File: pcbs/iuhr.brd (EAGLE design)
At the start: 38.4 x 23 mm, 82 parts, among them Q1 20.000MHz, Q2 MOSFET-NCHANNELSMD

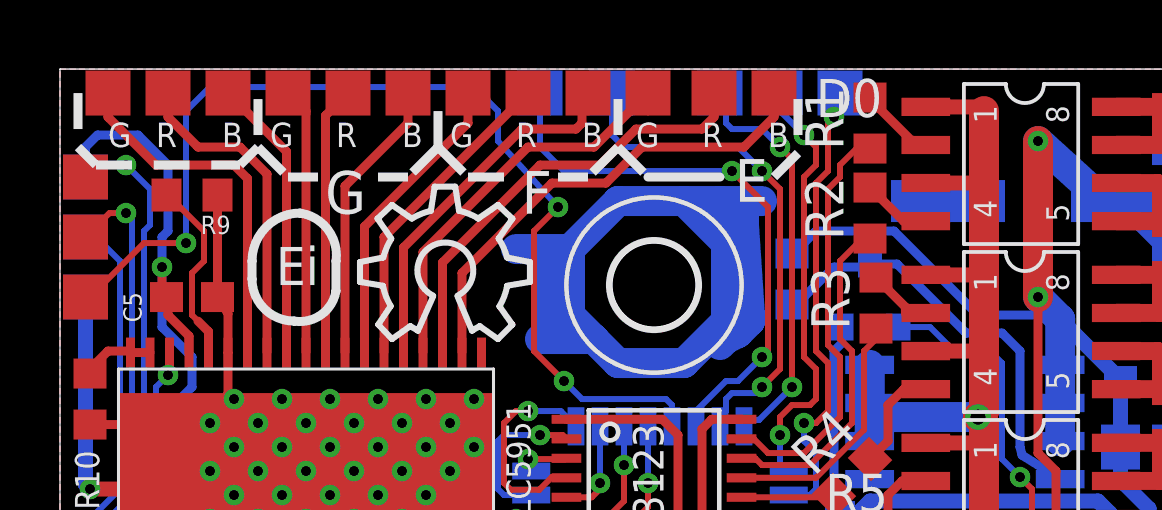
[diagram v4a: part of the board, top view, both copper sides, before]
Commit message: Add GND and +5V breakout pads.
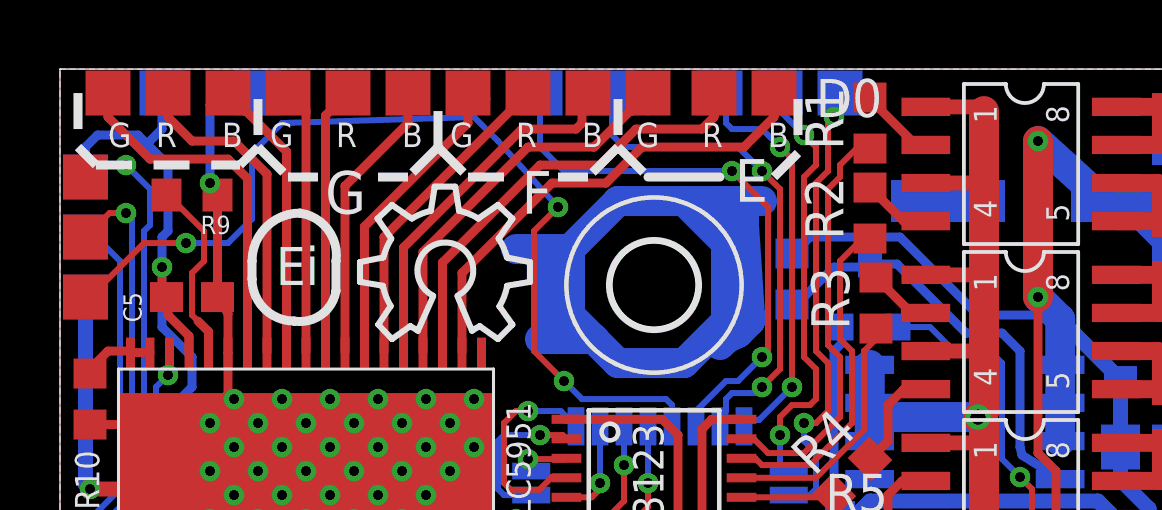
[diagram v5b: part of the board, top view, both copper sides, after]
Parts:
- added +5V, GND: TPTP15SQ, testpad:TP15SQ
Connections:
- net GND: now also GND.TP
- net VCC: now also +5V.TP
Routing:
- net GND: track 149.0 -> 155.2 mm, vias 41 -> 42
- net RESET: track 35.5 -> 32.7 mm
- net VCC: track 65.3 -> 67.2 mm
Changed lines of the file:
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@@
 <text x="38.2" y="21.4" size="0.8128" layer="26" rot="MR0">+12V</text>
 <text x="38" y="12.8" size="0.8128" layer="26" rot="MR0">GND</text>
-<text x="24.2" y="15.6" size="0.8128" layer="26" rot="MR90">Encoder</text>
+<text x="26.4" y="19" size="0.8128" layer="26" rot="MR0">Encoder</text>
 <wire x1="21" y1="22.2" x2="21" y2="20.2" width="0.3" layer="26" style="shortdash"/>
 <wire x1="21" y1="20.2" x2="21.8" y2="19.4" width="0.3" layer="26" style="shortdash"/>
@@
 <wire x1="10.6" y1="22.6" x2="10.6" y2="22" width="0.3" layer="26"/>
 <wire x1="10.6" y1="22" x2="11.2" y2="21.4" width="0.3" layer="26"/>
-<text x="14.8" y="0.4" size="0.8128" layer="26" rot="MR35">https://github.com/ekiwi/iuhr</text>
+<text x="12.8" y="0.6" size="0.6096" layer="26" rot="MR35">https://github.com/ekiwi/iuhr</text>
 <text x="5.2" y="16.8" size="0.8128" layer="26" rot="MR180">(C) eKiwi 2013</text>
 <text x="6" y="15.2" size="0.8128" layer="26" rot="MR180">licensed under
@@
 <text x="21.4" y="20.4" size="0.8128" layer="25">R</text>
 <text x="23.6" y="20.4" size="0.8128" layer="25">B</text>
-<text x="11.8" y="18.4" size="0.8128" layer="26" rot="MR0">powered by
+<text x="13.4" y="17.6" size="0.8128" layer="26" rot="MR0">powered by
 xpcc</text>
+<wire x1="3.6" y1="21.4" x2="4.4" y2="20.6" width="0.3" layer="22"/>
+<wire x1="4.4" y1="20.6" x2="4.4" y2="19.8" width="0.3" layer="22"/>
+<wire x1="4.4" y1="19.8" x2="4" y2="20.2" width="0.3" layer="22"/>
+<wire x1="4.4" y1="19.8" x2="4.8" y2="20.2" width="0.3" layer="22"/>
+<wire x1="6.6" y1="21.4" x2="6.6" y2="20" width="0.3" layer="22"/>
+<wire x1="7" y1="20" x2="6.2" y2="20" width="0.3" layer="22"/>
 </plain>
 <attributes>
@@
 <element name="R7" library="resistor" package="R0603" value="33" x="27.2" y="3.6" rot="R270"/>
 <element name="R8" library="resistor" package="R0603" value="33" x="24" y="4.4" rot="R270"/>
+<element name="+5V" library="testpad" package="TP15SQ" value="TPTP15SQ" x="3.4" y="22.2" smashed="yes" rot="MR0">
+<attribute name="TP_SIGNAL_NAME" value="" x="3.4" y="19.66" size="1" layer="38" rot="MR0"/>
+<attribute name="NAME" x="2.1501" y="21.6001" size="0.8128" layer="26" rot="MR0"/>
+<attribute name="VALUE" x="4.162" y="21.311" size="0.0254" layer="28" rot="MR0"/>
+</element>
+<element name="GND" library="testpad" package="TP15SQ" value="TPTP15SQ" x="6.6" y="22.2" smashed="yes" rot="MR0">
+<attribute name="TP_SIGNAL_NAME" value="" x="6.6" y="19.66" size="1" layer="38" rot="MR0"/>
+<attribute name="NAME" x="10.1501" y="21.8001" size="0.8128" layer="26" rot="MR0"/>
+<attribute name="VALUE" x="7.362" y="21.311" size="0.0254" layer="28" rot="MR0"/>
+</element>
 </elements>
 <signals>
@@
 <wire x1="30.85" y1="4.6" x2="30.85" y2="4.05" width="0.3" layer="16"/>
 <wire x1="30.85" y1="4.05" x2="30.4" y2="3.6" width="0.3" layer="16"/>
+<contactref element="GND" pad="TP"/>
+<wire x1="5.25" y1="18.8" x2="5.25" y2="19.15" width="0.3" layer="1"/>
+<wire x1="5.25" y1="19.15" x2="5" y2="19.2" width="0.3" layer="1"/>
+<via x="5" y="19.2" extent="1-16" drill="0.3302"/>
+<wire x1="5.2" y1="22" x2="6.6" y2="22.2" width="0.3" layer="16"/>
+<wire x1="5" y1="19.2" x2="5" y2="21.8" width="0.3" layer="16"/>
+<wire x1="5" y1="21.8" x2="6.6" y2="22.2" width="0.3" layer="16"/>
 </signal>
 <signal name="VCC">
@@
 <wire x1="3.4" y1="17.4" x2="3.6" y2="17.6" width="0.3" layer="16"/>
 <wire x1="3.6" y1="17.6" x2="3.6" y2="19.8" width="0.3" layer="16"/>
-<wire x1="3.6" y1="19.8" x2="2.6" y2="20.8" width="0.3" layer="16"/>
+<wire x1="3.6" y1="19.8" x2="2.9" y2="20.5" width="0.3" layer="16"/>
+<wire x1="2.9" y1="20.5" x2="2.6" y2="20.8" width="0.3" layer="16"/>
 <wire x1="2.6" y1="20.8" x2="1.25" y2="20.8" width="0.3" layer="16"/>
 <wire x1="1.25" y1="20.8" x2="0.85" y2="20.4" width="0.3" layer="16"/>
@@
 <wire x1="25" y1="5.8" x2="25.45" y2="5.8" width="0.3" layer="16"/>
 <wire x1="25.45" y1="5.8" x2="26" y2="6.35" width="0.3" layer="16"/>
+<contactref element="+5V" pad="TP"/>
+<wire x1="3.4" y1="22.2" x2="3.4" y2="21" width="0.3" layer="16"/>
+<wire x1="3.4" y1="21" x2="2.9" y2="20.5" width="0.3" layer="16"/>
 </signal>
 <signal name="RESET">
@@
 <wire x1="2.8" y1="17.2" x2="4.2" y2="17.2" width="0.2" layer="1"/>
 <wire x1="0.85" y1="15.65" x2="0.85" y2="15.4" width="0.2" layer="1"/>
-<wire x1="4.2" y1="17.2" x2="4.2" y2="21.6" width="0.2" layer="16"/>
-<wire x1="4.2" y1="21.6" x2="5" y2="22.4" width="0.2" layer="16"/>
-<wire x1="5" y1="22.4" x2="13.8" y2="22.4" width="0.2" layer="16"/>
-<wire x1="13.8" y1="22.4" x2="14.6" y2="21.6" width="0.2" layer="16"/>
-<wire x1="14.6" y1="21.6" x2="14.6" y2="20.6" width="0.2" layer="16"/>
+<wire x1="7.4" y1="21.2" x2="13.8" y2="21.4" width="0.2" layer="16"/>
+<wire x1="13.8" y1="21.4" x2="14.6" y2="20.6" width="0.2" layer="16"/>
 <wire x1="17.4" y1="12" x2="16.8" y2="12.6" width="0.2" layer="16"/>
 <via x="16.8" y="12.6" extent="1-16" drill="0.3302"/>
@@
 <via x="16.6" y="18.4" extent="1-16" drill="0.3302"/>
 <wire x1="16.6" y1="18.4" x2="14.6" y2="20.6" width="0.2" layer="16"/>
+<wire x1="4.2" y1="17.2" x2="5.6" y2="17.2" width="0.2" layer="16"/>
+<wire x1="5.6" y1="17.2" x2="6.4" y2="18" width="0.2" layer="16"/>
+<wire x1="6.4" y1="18" x2="6.4" y2="20.2" width="0.2" layer="16"/>
+<wire x1="6.4" y1="20.2" x2="7.4" y2="21.2" width="0.2" layer="16"/>
 </signal>
 <signal name="N$2">
@@
 <contactref element="XR" pad="TP"/>
 <contactref element="TLC5951" pad="31"/>
-<wire x1="4.6" y1="20.4" x2="3.6" y2="21.4" width="0.3" layer="1"/>
+<wire x1="4.4" y1="20.6" x2="3.6" y2="21.4" width="0.3" layer="1"/>
 <wire x1="3.6" y1="21.4" x2="3.6" y2="22.2" width="0.3" layer="1"/>
 <wire x1="6.9" y1="13.55" x2="6.9" y2="19.5" width="0.3" layer="1"/>
-<wire x1="6.9" y1="19.5" x2="6" y2="20.4" width="0.3" layer="1"/>
-<wire x1="6" y1="20.4" x2="4.6" y2="20.4" width="0.3" layer="1"/>
+<wire x1="6.9" y1="19.5" x2="5.8" y2="20.6" width="0.3" layer="1"/>
+<wire x1="5.8" y1="20.6" x2="4.4" y2="20.6" width="0.3" layer="1"/>
 </signal>
 <signal name="N$27">
@@
 <contactref element="TLC5951" pad="32"/>
 <wire x1="1.6" y1="22.2" x2="1.6" y2="21.4" width="0.3" layer="1"/>
-<wire x1="1.6" y1="21.4" x2="3.2" y2="19.8" width="0.3" layer="1"/>
+<wire x1="1.6" y1="21.4" x2="3" y2="20" width="0.3" layer="1"/>
 <wire x1="6.25" y1="13.55" x2="6.25" y2="19.35" width="0.3" layer="1"/>
-<wire x1="6.25" y1="19.35" x2="5.8" y2="19.8" width="0.3" layer="1"/>
-<wire x1="5.8" y1="19.8" x2="3.2" y2="19.8" width="0.3" layer="1"/>
+<wire x1="6.25" y1="19.35" x2="5.6" y2="20" width="0.3" layer="1"/>
+<wire x1="5.6" y1="20" x2="3" y2="20" width="0.3" layer="1"/>
 </signal>
 <signal name="N$28">
@@
 <wire x1="34.15" y1="1" x2="33.2" y2="1" width="0.2" layer="16"/>
 <via x="33.2" y="1" extent="1-16" drill="0.3302"/>
-<wire x1="27.8" y1="17.6" x2="30.6" y2="14.8" width="0.3" layer="16"/>
+<wire x1="28" y1="17.4" x2="30.6" y2="14.8" width="0.3" layer="16"/>
 <wire x1="30.6" y1="14.8" x2="33.2" y2="14.8" width="0.3" layer="16"/>
 <wire x1="33.2" y1="14.8" x2="33.34" y2="14.66" width="0.3" layer="16"/>
@@
 <wire x1="37.4" y1="16.8" x2="35.6" y2="18.6" width="1" layer="16"/>
 <wire x1="24.4" y1="16.85" x2="24.45" y2="16.85" width="0.3" layer="16"/>
-<wire x1="24.45" y1="16.85" x2="25.2" y2="17.6" width="0.3" layer="16"/>
-<wire x1="25.2" y1="17.6" x2="27.8" y2="17.6" width="0.3" layer="16"/>
+<wire x1="24.45" y1="16.85" x2="25" y2="17.4" width="0.3" layer="16"/>
+<wire x1="25" y1="17.4" x2="28" y2="17.4" width="0.3" layer="16"/>
 <wire x1="35.6" y1="18.6" x2="34.8" y2="18.6" width="1" layer="16"/>
 <wire x1="34.8" y1="18.6" x2="32.6" y2="20.6" width="1" layer="16"/>
